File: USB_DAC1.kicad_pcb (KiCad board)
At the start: 2 copper layers, 97.8 x 70.4 mm, 91 parts, among them J1 USB_OTG, J2 Audio-Jack-3, J3 Audio-Jack-4, U1 PCM2704DB, U2 MC78M05CDT, U3 MC78M05CDT, U4 OPA2340, U5 OPA2340, U6 OPA2340, Y1 Crystal

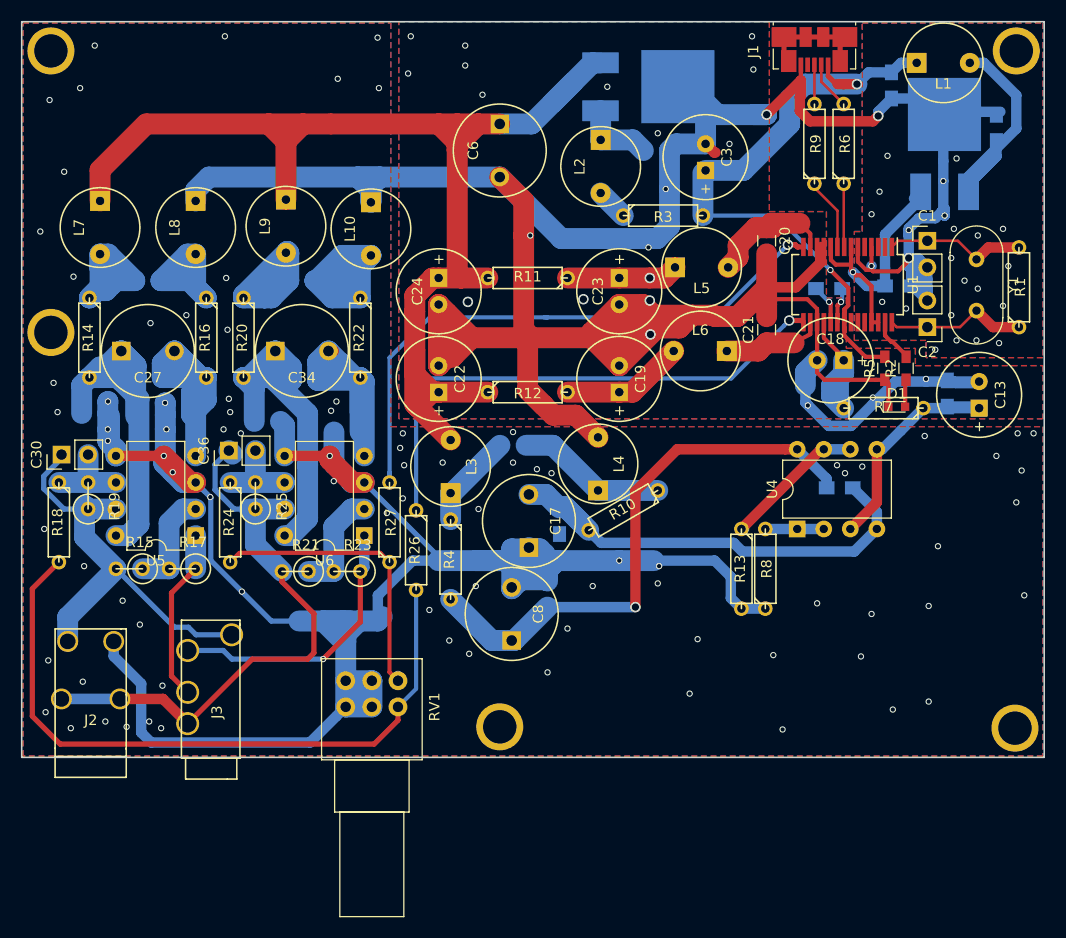
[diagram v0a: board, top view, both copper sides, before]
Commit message: C18 C17 C8が干渉してた問題の修正 部品表の追加
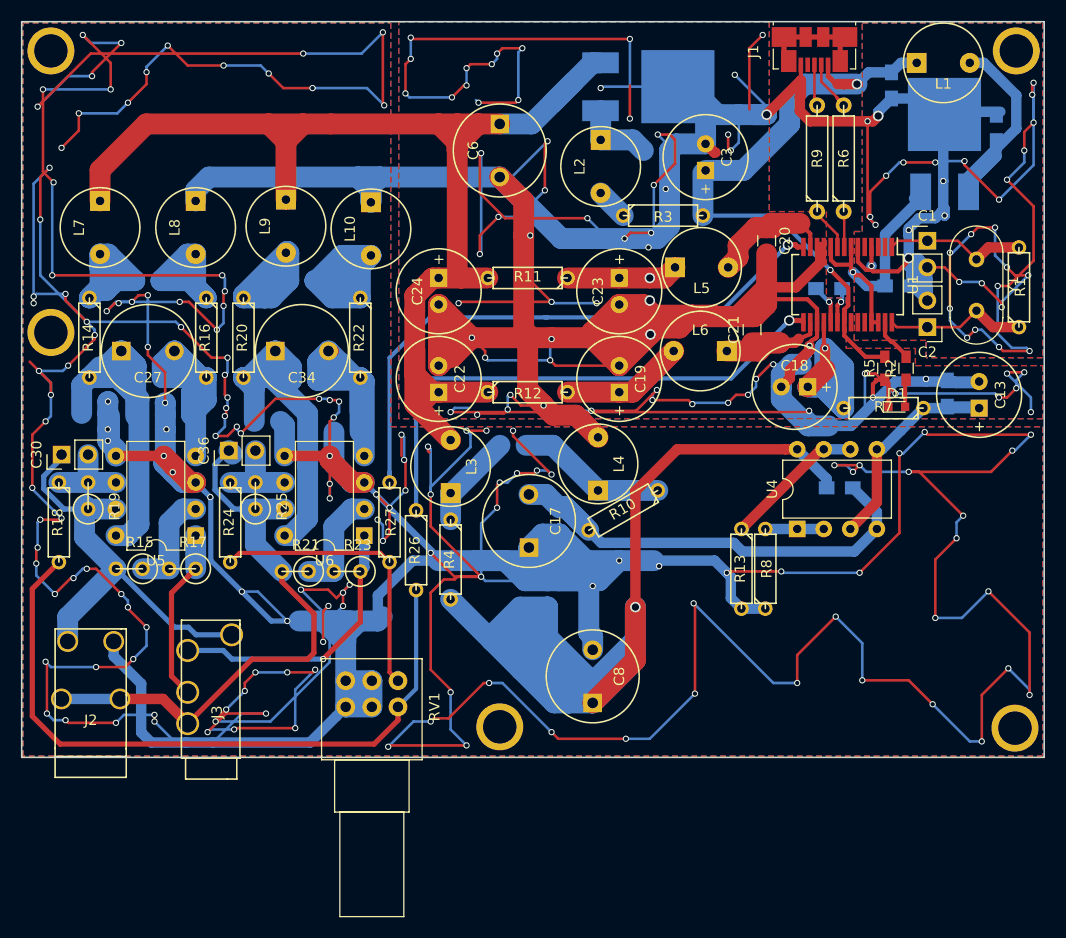
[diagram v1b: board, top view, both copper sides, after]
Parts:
- R6, R9: footprint Discret:R3 -> Discret:R4
- moved C8 9.78 mm to (156.6, 106.6)
- moved C18 4.27 mm to (175.9, 78.9)
- moved C12 2.07 mm to (177.8, 76.7)
- moved R9 1.42 mm to (178.1, 57.0)
- moved C21 1.40 mm to (171.8, 73.4)
- moved R6 1.40 mm to (180.6, 57.0)
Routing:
- net GND: track 213.9 -> 987.3 mm, vias 12 -> 154
- net GNDA: track 362.5 -> 775.0 mm, vias 15 -> 96
- net Net-(C10-Pad1): track 54.1 -> 134.9 mm
- net Net-(C12-Pad1): track 14.5 -> 33.2 mm, vias 0 -> 1
- net (no net): track 0.00 -> 10.8 mm, vias 107 -> 2
- net Net-(C21-Pad1): track 9.65 -> 13.3 mm
- net Net-(R9-Pad1): track 6.96 -> 4.19 mm
- net Net-(R6-Pad1): track 6.08 -> 3.49 mm
- net Net-(J1-Pad2): track 4.64 -> 5.66 mm
- net Net-(J1-Pad3): track 3.75 -> 4.62 mm
